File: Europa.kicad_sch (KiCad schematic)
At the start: 0 parts

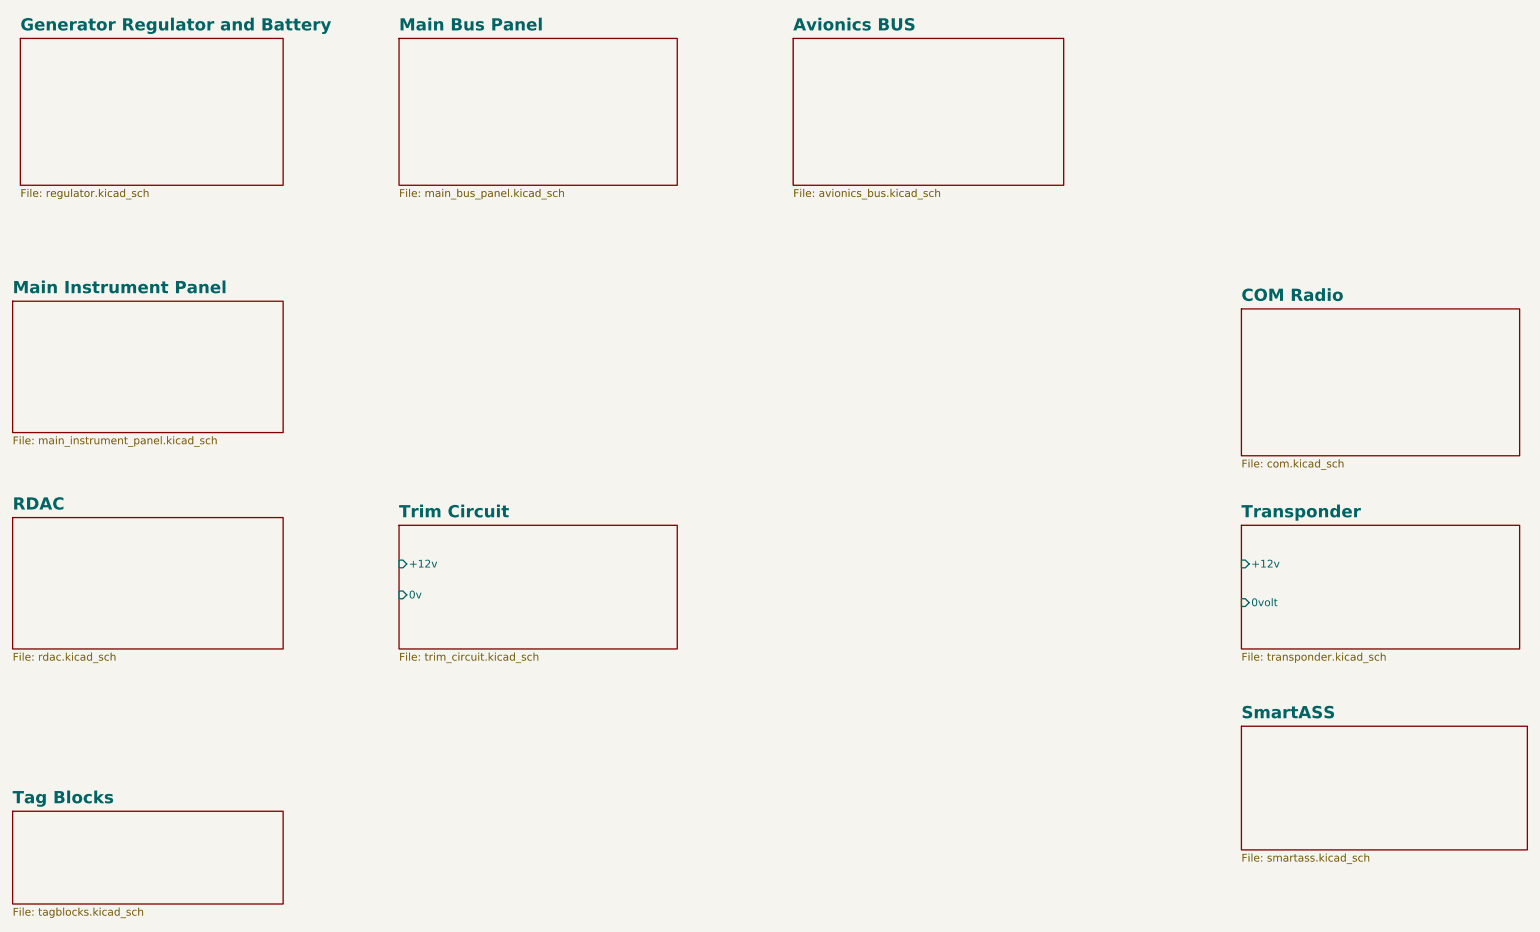
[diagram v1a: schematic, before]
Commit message: Added Connectors sheet
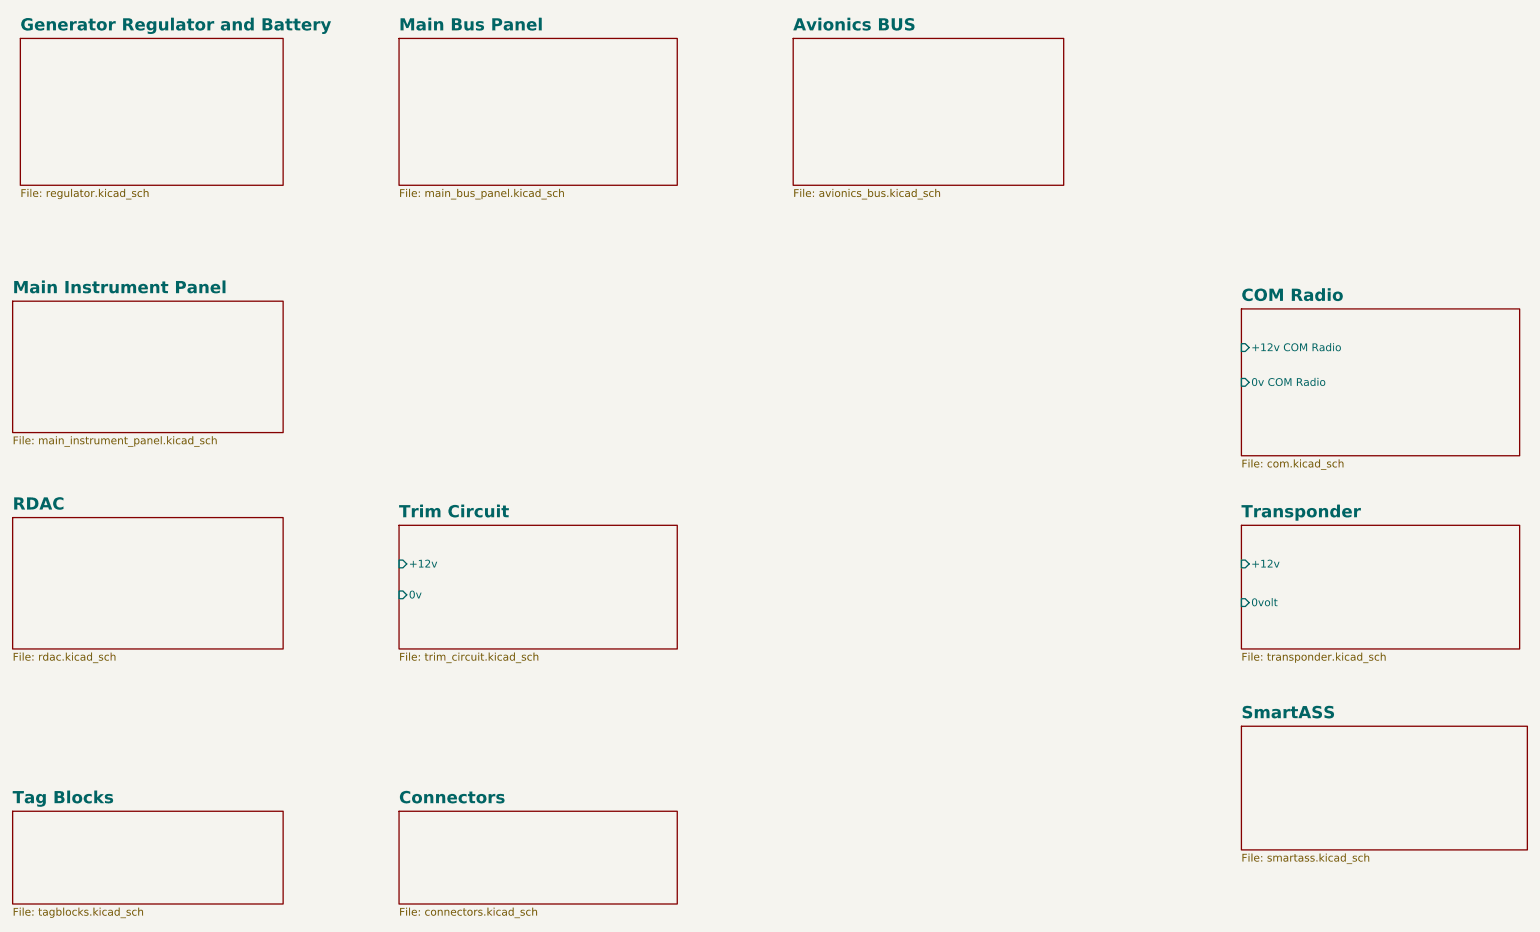
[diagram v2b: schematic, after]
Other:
- added sheet Connectors (connectors.kicad_sch)
- sheet COM Radio ports: added +12v COM Radio, 0v COM Radio; removed none
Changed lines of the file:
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@@
     (rev "1")
+  )
+  (sheet (at 92.71 156.21) (size 45.72 15.24) (fields_autoplaced)
+    (stroke (width 0.1524) (type solid) (color 0 0 0 0))
+    (fill (color 0 0 0 0.0000))
+    (property "Sheet name" "Connectors" (id 0) (at 92.71 155.1334 0)
+      (effects (font (size 2 2) bold) (justify left bottom))
+    )
+    (property "Sheet file" "connectors.kicad_sch" (id 1) (at 92.71 172.0346 0)
+      (effects (font (size 1.27 1.27)) (justify left top))
+    )
   )
   (sheet (at 231.14 109.22) (size 45.72 20.32) (fields_autoplaced)
@@
     (property "Sheet file" "com.kicad_sch" (id 1) (at 231.14 98.3746 0)
       (effects (font (size 1.27 1.27)) (justify left top))
+    )
+    (pin "0v COM Radio" input (at 231.14 85.725 180)
+      (effects (font (size 1.27 1.27)) (justify left))
+    )
+    (pin "+12v COM Radio" input (at 231.14 80.01 180)
+      (effects (font (size 1.27 1.27)) (justify left))
     )
   )
@@
     (path "/e1ebce97-45bd-4d6d-8f32-43a2d30fa366" (page "10"))
     (path "/e1ffd005-c35b-448a-8691-6cad5a2d74ae" (page "11"))
+    (path "/1c871bc4-f2ef-4ec4-b2d7-f28c56def7ce" (page "12"))
   )
   (symbol_instances
@@
       (reference "Lamps-CB") (unit 1) (value "CircuitBreaker_1P") (footprint "")
     )
+    (path "/1c871bc4-f2ef-4ec4-b2d7-f28c56def7ce/e78129cd-a963-4a8d-b873-8639a2170741"
+      (reference "PL1") (unit 1) (value "COM Radio Power") (footprint "")
+    )
     (path "/5afc04a8-14bc-4c25-8a7e-c4e01fd6c06c/e4be1ad4-ea4e-4e5e-a9ae-3dbf40ca29ce"
       (reference "PL1-A") (unit 1) (value "Conn_01x02_Female") (footprint "")
@@
       (reference "PL1A") (unit 1) (value "Conn_01x03_Female") (footprint "")
     )
+    (path "/1c871bc4-f2ef-4ec4-b2d7-f28c56def7ce/6f915348-9b0f-4589-8cc5-b6b947470487"
+      (reference "PL2") (unit 1) (value "Avionics Master Switch") (footprint "")
+    )
     (path "/5afc04a8-14bc-4c25-8a7e-c4e01fd6c06c/b42ac1f6-59d0-4f2c-85ba-9a1f496fb2b0"
       (reference "PL2") (unit 1) (value "Conn_01x02_Female") (footprint "")
@@
       (reference "PL2") (unit 1) (value "Conn_01x02_Male") (footprint "")
     )
+    (path "/1c871bc4-f2ef-4ec4-b2d7-f28c56def7ce/fe9d6189-0c17-449b-a1a2-9797f0acc8ed"
+      (reference "PL3") (unit 1) (value "ECB") (footprint "")
+    )
     (path "/c5676131-d5a4-4fde-914f-3f396c9cd255/d008d60e-b61b-4155-beb9-5029ffe66249"
       (reference "PL3A") (unit 1) (value "DB9_Male") (footprint "")
@@
       (reference "PL3B") (unit 1) (value "DB9_Female") (footprint "")
     )
+    (path "/1c871bc4-f2ef-4ec4-b2d7-f28c56def7ce/63c8bb49-4a54-4d8e-b462-3c0762621446"
+      (reference "PL4") (unit 1) (value "Trim Power") (footprint "")
+    )
+    (path "/1c871bc4-f2ef-4ec4-b2d7-f28c56def7ce/d7b64594-c4c5-4190-88ee-8e7d3cb128bf"
+      (reference "PL5") (unit 1) (value "Trim Servo") (footprint "")
+    )
+    (path "/1c871bc4-f2ef-4ec4-b2d7-f28c56def7ce/bfe49bb9-e825-41b6-963d-c95a2519465f"
+      (reference "PL6") (unit 1) (value "TC90 Control Head") (footprint "")
+    )
+    (path "/1c871bc4-f2ef-4ec4-b2d7-f28c56def7ce/83b6a868-147c-46b4-ac8a-fe11abd5d170"
+      (reference "PL7") (unit 1) (value "MGL Oil Temp & Press") (footprint "")
+    )
+    (path "/1c871bc4-f2ef-4ec4-b2d7-f28c56def7ce/feb536dc-0816-4494-a9c2-a7b9cd5ce990"
+      (reference "PL8") (unit 1) (value "MGL EFIS") (footprint "")
+    )
+    (path "/1c871bc4-f2ef-4ec4-b2d7-f28c56def7ce/16239128-b9d6-4032-a671-0433740bc7f6"
+      (reference "PL9") (unit 1) (value "Instrument Panel") (footprint "")
+    )
     (path "/c5676131-d5a4-4fde-914f-3f396c9cd255/559ccf97-058c-431a-aa6c-8b448def102e"
       (reference "PL9-A") (unit 1) (value "DB15_Female") (footprint "")
@@
       (reference "PL9/9") (unit 1) (value "Conn_01x01") (footprint "")
     )
+    (path "/1c871bc4-f2ef-4ec4-b2d7-f28c56def7ce/c7f3f682-9108-4543-b76a-8d6f8e6c219a"
+      (reference "PL12") (unit 1) (value "Current Sensor") (footprint "")
+    )
     (path "/a5352cd5-5c6a-411a-b1fe-0b8c42ec40dc/2409a3e3-f0dc-4e5d-8d6e-71c8c1c58eb7"
       (reference "PL12/1") (unit 1) (value "Conn_01x01") (footprint "")
@@
       (reference "PL15") (unit 1) (value "PL15/1") (footprint "")
     )
+    (path "/1c871bc4-f2ef-4ec4-b2d7-f28c56def7ce/fe076a36-c316-45a1-8f21-17de69074d5f"
+      (reference "PL15") (unit 1) (value "Instrument Module") (footprint "")
+    )
     (path "/95e96eec-8054-412c-b439-e274da9864da/3d5cbab8-4231-4f47-97f4-fa9a7735ee55"
       (reference "PL15/1") (unit 1) (value "Conn_01x01") (footprint "")
@@
       (reference "PL15/10") (unit 1) (value "Conn_01x01") (footprint "")
     )
+    (path "/1c871bc4-f2ef-4ec4-b2d7-f28c56def7ce/4af967dc-7df1-4a77-a173-6be423bfc848"
+      (reference "PL16") (unit 1) (value "Transponder") (footprint "")
+    )
     (path "/293b5c94-66ed-4931-a87f-688673218b15/ebe3f642-9b43-430a-b037-7f70139ef68a"
       (reference "PL16") (unit 1) (value "DB15_Female") (footprint "")
     )
+    (path "/1c871bc4-f2ef-4ec4-b2d7-f28c56def7ce/c35308fb-7500-4147-ae38-7e02b5a8317c"
+      (reference "PL20") (unit 1) (value "Headset Panel") (footprint "")
+    )
     (path "/e876c59e-4288-4b76-b538-81605be93f21/02428102-6ae6-4d41-9989-a38e205d44b5"

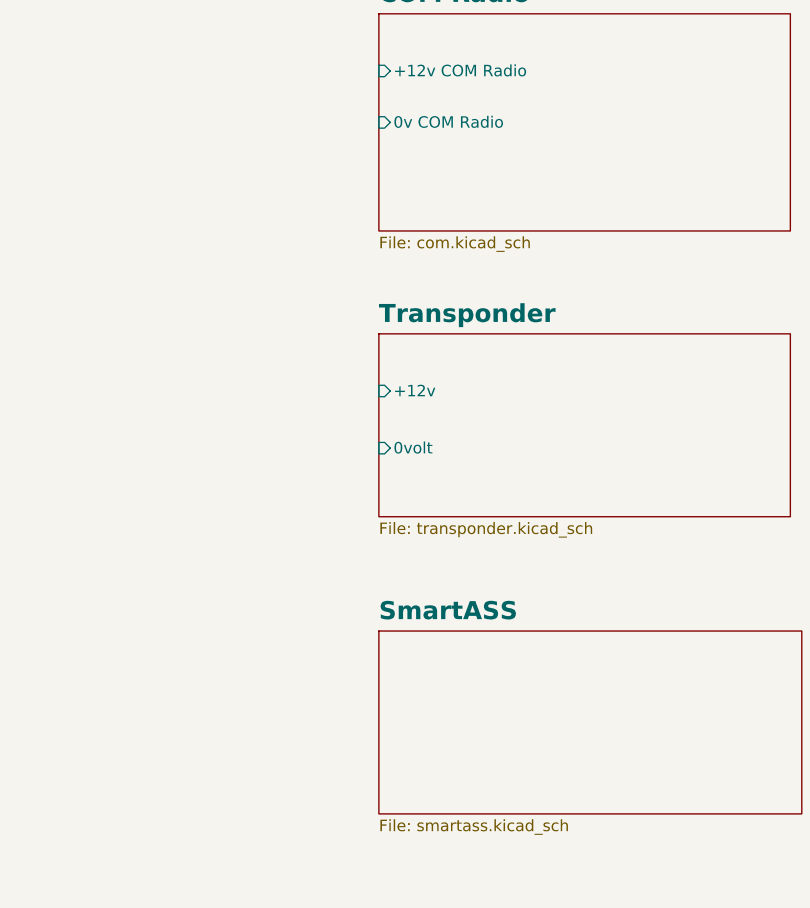
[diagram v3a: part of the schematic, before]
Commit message: Small updates to multiple sheets, and major update to SmartAss sheet
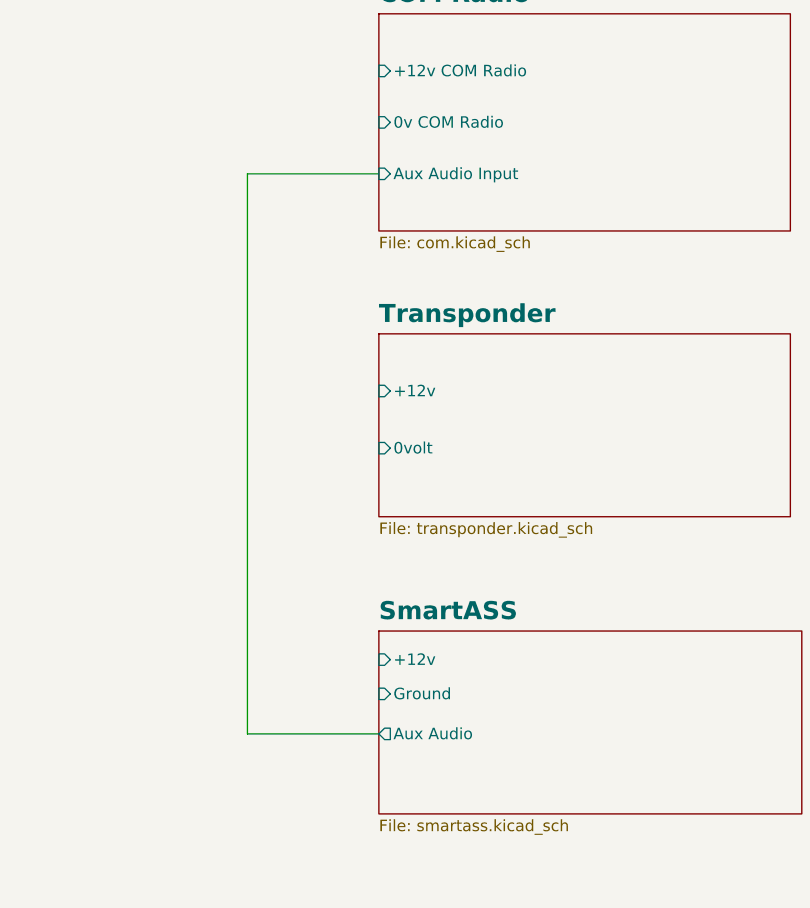
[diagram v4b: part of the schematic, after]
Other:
- sheet COM Radio ports: added Aux Audio Input; removed none
- sheet SmartASS ports: added +12v, Aux Audio, Ground; removed none
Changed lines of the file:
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@@
     (rev "1")
   )
+  (wire (pts (xy 216.535 153.67) (xy 231.14 153.67))
+    (stroke (width 0) (type default) (color 0 0 0 0))
+  )
+  (wire (pts (xy 216.535 91.44) (xy 216.535 153.67))
+    (stroke (width 0) (type default) (color 0 0 0 0))
+  )
+  (wire (pts (xy 231.14 91.44) (xy 216.535 91.44))
+    (stroke (width 0) (type default) (color 0 0 0 0))
+  )
   (sheet (at 92.71 156.21) (size 45.72 15.24) (fields_autoplaced)
     (stroke (width 0.1524) (type solid) (color 0 0 0 0))
@@
       (effects (font (size 1.27 1.27)) (justify left))
     )
+    (pin "Aux Audio Input" input (at 231.14 91.44 180)
+      (effects (font (size 1.27 1.27)) (justify left))
+    )
   )
   (sheet (at 92.71 109.22) (size 45.72 20.32) (fields_autoplaced)
@@
     (property "Sheet file" "smartass.kicad_sch" (id 1) (at 231.14 163.1446 0)
       (effects (font (size 1.27 1.27)) (justify left top))
+    )
+    (pin "Aux Audio" output (at 231.14 153.67 180)
+      (effects (font (size 1.27 1.27)) (justify left))
+    )
+    (pin "+12v" input (at 231.14 145.415 180)
+      (effects (font (size 1.27 1.27)) (justify left))
+    )
+    (pin "Ground" input (at 231.14 149.225 180)
+      (effects (font (size 1.27 1.27)) (justify left))
     )
   )
@@
       (reference "J?") (unit 1) (value "HeadPhone 1") (footprint "")
     )
-    (path "/75f9b772-c578-422e-a634-635b5097c8a8/365f6a8d-f5a2-4142-886f-1ce22a494b7c"
-      (reference "J?") (unit 1) (value "DB15_Male") (footprint "")
-    )
     (path "/866b3cfa-81f9-4c05-8259-46d4a400c4a9/3fd3a499-d077-4b88-94d8-a82d86dba2b8"
       (reference "J?") (unit 1) (value "PL5-A") (footprint "")
@@
       (reference "J?") (unit 1) (value "PL?-B") (footprint "")
     )
+    (path "/e1ebce97-45bd-4d6d-8f32-43a2d30fa366/68d5e530-46f6-4d76-abef-febf18aab817"
+      (reference "J?") (unit 1) (value "DB15_Female") (footprint "")
+    )
     (path "/75f9b772-c578-422e-a634-635b5097c8a8/6e0ab079-c6a2-416c-ac49-805bc6027b3f"
       (reference "J?") (unit 1) (value "MIC 1") (footprint "")
@@
       (reference "J?") (unit 1) (value "PL1-A") (footprint "")
     )
+    (path "/e1ebce97-45bd-4d6d-8f32-43a2d30fa366/8fb2c536-d5fc-4d74-bad2-e79e4b836792"
+      (reference "J?") (unit 1) (value "DB15_Male") (footprint "")
+    )
     (path "/75f9b772-c578-422e-a634-635b5097c8a8/94337d76-ba27-4669-8209-0ee5ee3b3283"
       (reference "J?") (unit 1) (value "PL?-A") (footprint "")
@@
       (reference "PL5") (unit 1) (value "Trim Servo") (footprint "")
     )
+    (path "/75f9b772-c578-422e-a634-635b5097c8a8/365f6a8d-f5a2-4142-886f-1ce22a494b7c"
+      (reference "PL6") (unit 1) (value "DB15_Male") (footprint "")
+    )
     (path "/1c871bc4-f2ef-4ec4-b2d7-f28c56def7ce/bfe49bb9-e825-41b6-963d-c95a2519465f"
       (reference "PL6") (unit 1) (value "TC90 Control Head") (footprint "")
@@
       (reference "PL15/6") (unit 1) (value "Conn_01x01") (footprint "")
     )
+    (path "/e1ebce97-45bd-4d6d-8f32-43a2d30fa366/e012a903-4fbd-4e81-80ee-14895e0b8b00"
+      (reference "PL15/6") (unit 1) (value "Conn_01x01") (footprint "")
+    )
     (path "/95e96eec-8054-412c-b439-e274da9864da/1c9a909b-961c-49c2-879c-f646c2a2f1a5"
       (reference "PL15/9") (unit 1) (value "Conn_01x01") (footprint "")
@@
       (reference "TB6") (unit 1) (value "Screw_Terminal_01x12") (footprint "")
     )
+    (path "/e1ebce97-45bd-4d6d-8f32-43a2d30fa366/62bd0e62-efef-48fe-bf5d-fcf6492904de"
+      (reference "TY91/20") (unit 1) (value "Aux Audio") (footprint "")
+    )
     (path "/e876c59e-4288-4b76-b538-81605be93f21/3a4078e7-24de-4bfd-a13a-9bee3112ef73"
